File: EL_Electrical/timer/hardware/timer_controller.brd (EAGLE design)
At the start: 44 x 36 mm, 25 parts, among them IC2 TC4S584F, IC3 TC4S584F, IC4 LM555D, J1 22-27-2041-04, Q1 BSS138, T1 2N2369

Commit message: Change footprint for 150uF capacitor. Rearrange text infos. Add a GND test pin
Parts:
- added GND: GND, pinhead:1X01
- C2: device rcl:C0805 -> rcl:153CLV-0605
- moved C2 4.20 mm to (22.6, 27.4), turned to 270 degrees
- moved R10 0.25 mm to (15.3, 15.3)
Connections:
- net GND: now also C2.-, GND.1; no longer C2.2
- net TRIGGER: now also C2.+; no longer C2.1
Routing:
- net TRIGGER: track 14.3 -> 18.3 mm
- net N$17: track 13.2 -> 15.8 mm
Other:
- board text added: "Timer INVICTUS"

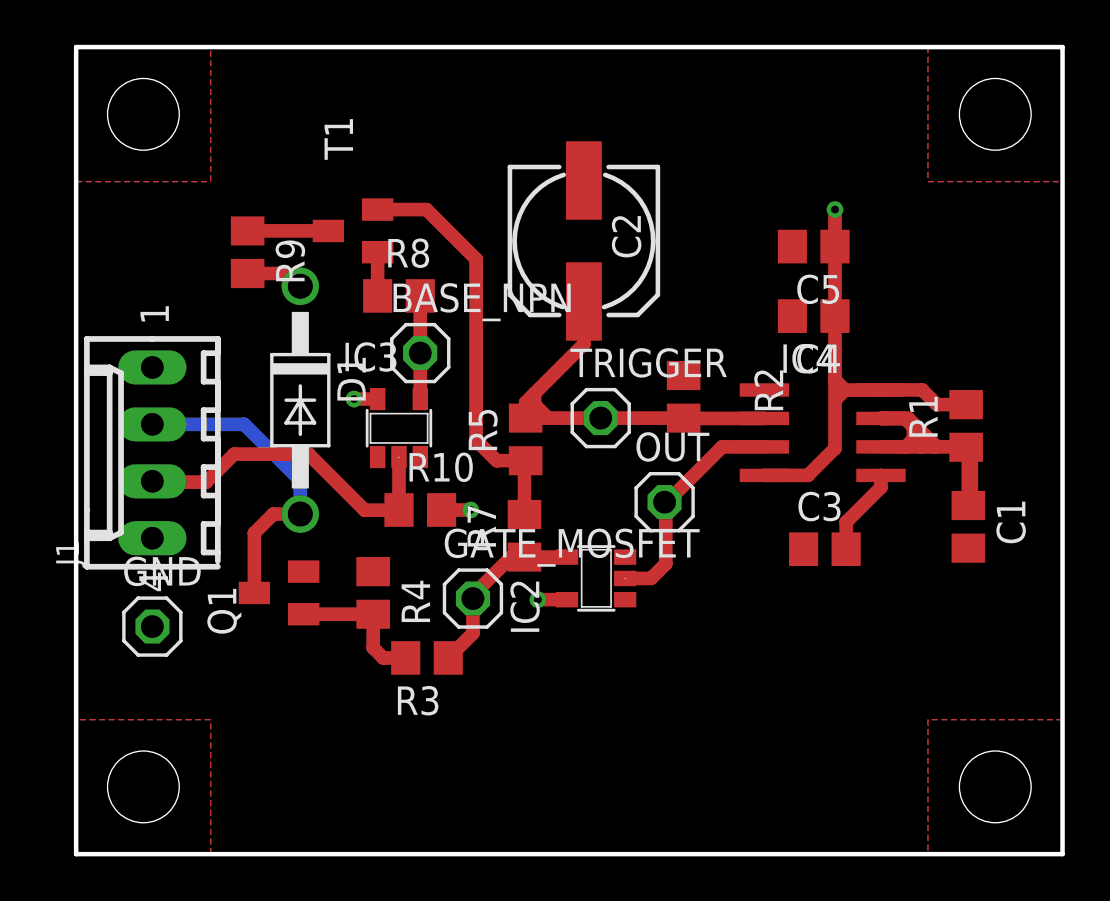
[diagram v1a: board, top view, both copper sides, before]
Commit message: Timer_controller add pin
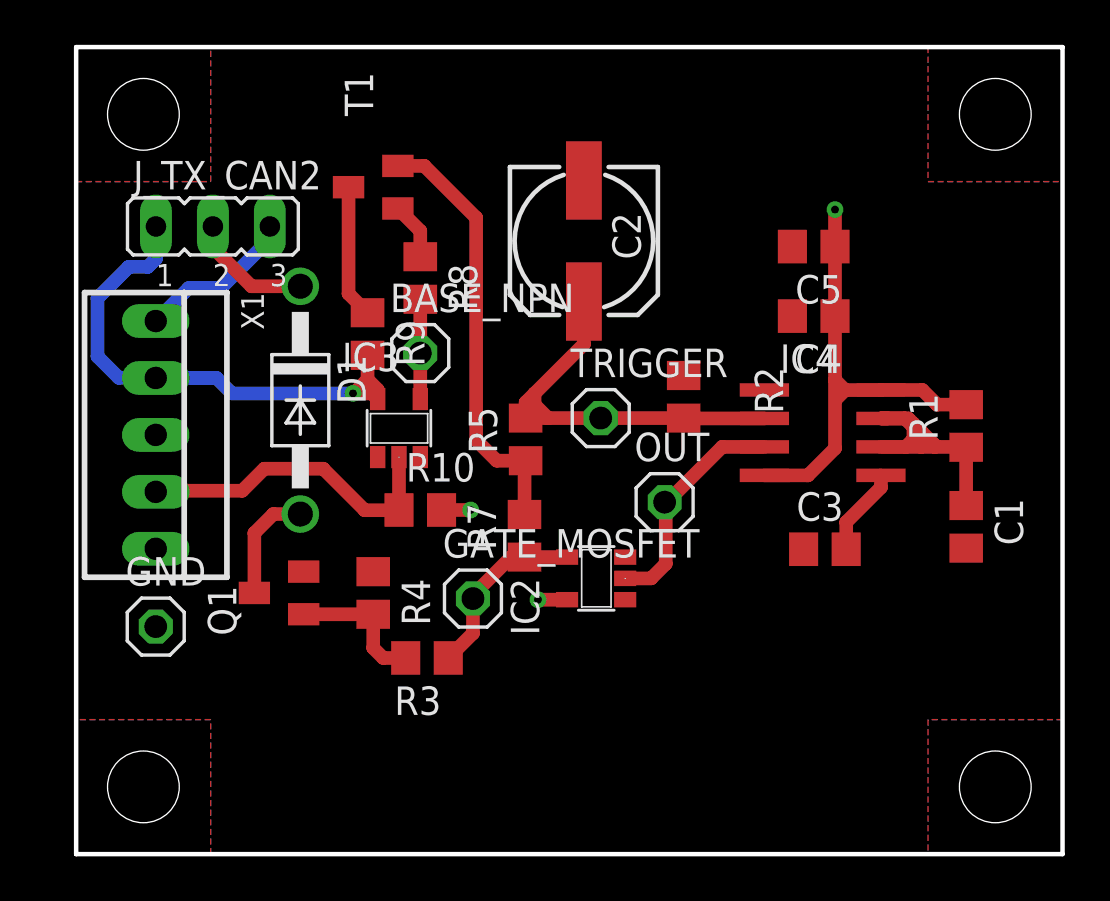
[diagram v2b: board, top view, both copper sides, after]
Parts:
- removed J1: 22-27-2041-04, con-molex:6410-04
- added J_TX_CAN2: (no value), jumper:JP2
- added X1: 22-23-2051, con-molex:22-23-2051
- moved R9 6.48 mm to (13.0, 23.2)
- moved T1 2.15 mm to (13.2, 29.8)
- moved R8 1.24 mm to (15.3, 25.7), turned to 270 degrees
- moved GND 0.15 mm to (3.55, 10.2)
- moved C1 0.10 mm to (39.7, 14.6)
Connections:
- new net 12_SWITCHES: J_TX_CAN2.3, X1.1
- new net RELAIS_INJECTEUR_12_PROTEGE: D1.C, J_TX_CAN2.2
- new net RELAIS_INJECTEUR_MASSE: D1.A, Q1.3
- net +12V: now also J_TX_CAN2.1, X1.2; no longer D1.C, J1.1
- net BP_START: now also X1.4; no longer J1.3
- net GND: now also X1.5; no longer J1.4
- net RELAIS_INJECTEUR: now also X1.3; no longer D1.A, J1.2, Q1.3
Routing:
- net +12V: track 27.4 -> 47.5 mm
- net RELAIS_INJECTEUR: track 14.2 -> 0.00 mm
- net 12_SWITCHES: track 0.00 -> 7.17 mm
- net RELAIS_INJECTEUR_12_PROTEGE: track 0.00 -> 5.56 mm
- net RELAIS_INJECTEUR_MASSE: track 0.00 -> 5.07 mm
- net N$2: track 3.60 -> 5.95 mm
- net N$17: track 15.8 -> 13.8 mm
- net N$26: track 18.4 -> 19.4 mm
- net N$27: track 1.95 -> 2.56 mm
- net BP_START: track 14.9 -> 14.4 mm
